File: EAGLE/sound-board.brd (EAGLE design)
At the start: 99.4 x 80 mm, 99 parts, among them IC1 SN76477, J0 POWER, J1 CON, J2 CON, J3 AUDIO, P10 1M, P2 1M, P3 1M, P4 1M, P6 50k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

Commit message: Minor modifications to PCB
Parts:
- added C27_THT: 10u, rcl:E2,5-5
- moved C27 1.27 mm to (10.2, 5.08), turned to 90 degrees
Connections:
- net GND: now also C27_THT.-
- net N$13: now also C27_THT.+
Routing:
- net N$13: track 5.40 -> 14.1 mm
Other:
- board text added: "SN76477 Sound Board 2018 Daniel Rojas"
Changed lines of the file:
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@@
 <dimension x1="0" y1="0" x2="0" y2="79.375" x3="-25.4" y3="39.6875" textsize="1.778" layer="47" visible="yes"/>
 <dimension x1="0" y1="0" x2="99.695" y2="0" x3="49.8475" y3="-19.05" textsize="1.778" layer="47" visible="yes"/>
+<text x="60.96" y="20.32" size="1.27" layer="25">SN76477 Sound Board
+2018 Daniel Rojas</text>
 </plain>
 <attributes>
@@
 <elements>
 <element name="C1" library="rcl" library_urn="urn:adsk.eagle:library:334" package="C0805" package3d_urn="urn:adsk.eagle:package:23617/2" value="150p" x="10.16" y="60.96" smashed="yes" rot="R180">
-<attribute name="VALUE" x="13.97" y="53.975" size="1.27" layer="27" rot="R180" align="bottom-right"/>
+<attribute name="VALUE" x="13.335" y="57.785" size="1.27" layer="27" rot="R180" align="bottom-right"/>
 </element>
 <element name="C10" library="rcl" library_urn="urn:adsk.eagle:library:334" package="C0805" package3d_urn="urn:adsk.eagle:package:23617/2" value="10u" x="10.16" y="45.72" smashed="yes" rot="R180">
@@
 </element>
 <element name="C2" library="rcl" library_urn="urn:adsk.eagle:library:334" package="C0805" package3d_urn="urn:adsk.eagle:package:23617/2" value="390p" x="10.16" y="63.5" smashed="yes" rot="R180">
-<attribute name="VALUE" x="13.97" y="55.88" size="1.27" layer="27" rot="R180" align="bottom-right"/>
+<attribute name="VALUE" x="13.335" y="59.69" size="1.27" layer="27" rot="R180" align="bottom-right"/>
 </element>
 <element name="C20" library="rcl" library_urn="urn:adsk.eagle:library:334" package="C0805" package3d_urn="urn:adsk.eagle:package:23617/2" value="10u" x="90.17" y="49.53" smashed="yes" rot="R180">
@@
 <attribute name="VALUE" x="86.36" y="2.54" size="1.27" layer="27" rot="R180"/>
 </element>
-<element name="C27" library="rcl" library_urn="urn:adsk.eagle:library:334" package="C0805" package3d_urn="urn:adsk.eagle:package:23617/2" value="10u" x="10.16" y="3.81" smashed="yes">
-<attribute name="VALUE" x="13.335" y="3.81" size="1.27" layer="27"/>
+<element name="C27" library="rcl" library_urn="urn:adsk.eagle:library:334" package="C0805" package3d_urn="urn:adsk.eagle:package:23617/2" value="10u" x="10.16" y="5.08" smashed="yes" rot="R90">
+<attribute name="VALUE" x="12.065" y="5.715" size="1.27" layer="27" rot="R270"/>
 </element>
 <element name="C3" library="rcl" library_urn="urn:adsk.eagle:library:334" package="C0805" package3d_urn="urn:adsk.eagle:package:23617/2" value="1n" x="10.16" y="66.04" smashed="yes" rot="R180">
-<attribute name="VALUE" x="13.97" y="57.785" size="1.27" layer="27" rot="R180" align="bottom-right"/>
+<attribute name="VALUE" x="13.335" y="67.945" size="1.27" layer="27" rot="R180" align="bottom-right"/>
 </element>
 <element name="C4" library="rcl" library_urn="urn:adsk.eagle:library:334" package="C0805" package3d_urn="urn:adsk.eagle:package:23617/2" value="10n" x="10.16" y="68.58" smashed="yes" rot="R180">
-<attribute name="VALUE" x="13.97" y="59.69" size="1.27" layer="27" rot="R180" align="bottom-right"/>
+<attribute name="VALUE" x="13.335" y="69.85" size="1.27" layer="27" rot="R180" align="bottom-right"/>
 </element>
 <element name="C5" library="rcl" library_urn="urn:adsk.eagle:library:334" package="C0805" package3d_urn="urn:adsk.eagle:package:23617/2" value="10n" x="10.16" y="33.02" smashed="yes" rot="R180">
@@
 <attribute name="VALUE" x="34.29" y="8.89" size="1.016" layer="27" ratio="10" rot="R180"/>
 </element>
+<element name="C27_THT" library="rcl" library_urn="urn:adsk.eagle:library:334" package="E2,5-5" package3d_urn="urn:adsk.eagle:package:23344/1" value="10u" x="16.51" y="5.08" smashed="yes" rot="R90"/>
 </elements>
 <signals>
@@
 </polygon>
 <via x="21.59" y="20.32" extent="1-16" drill="0.35"/>
+<contactref element="C27_THT" pad="-"/>
 </signal>
 <signal name="NOISE_OSC_RES">
@@
 <contactref element="C27" pad="1"/>
 <contactref element="CON_SPEAKER" pad="2"/>
-<wire x1="3.81" y1="3.81" x2="9.21" y2="3.81" width="0.8128" layer="1"/>
+<contactref element="C27_THT" pad="+"/>
+<wire x1="3.81" y1="3.81" x2="8.89" y2="3.81" width="0.8128" layer="1"/>
+<wire x1="8.89" y1="3.81" x2="9.84" y2="3.81" width="0.8128" layer="1"/>
+<wire x1="9.84" y1="3.81" x2="10.16" y2="4.13" width="0.8128" layer="1"/>
+<wire x1="8.89" y1="3.81" x2="16.51" y2="3.81" width="0.8128" layer="1"/>
 </signal>
 <signal name="N$60">
@@
 </drawing>
 <compatibility>
+<note version="6.3" minversion="6.2.2" severity="warning">
+Since Version 6.2.2 text objects can contain more than one line,
+which will not be processed correctly with this version.
+</note>
 <note version="8.2" severity="warning">
 Since Version 8.2, EAGLE supports online libraries. The ids

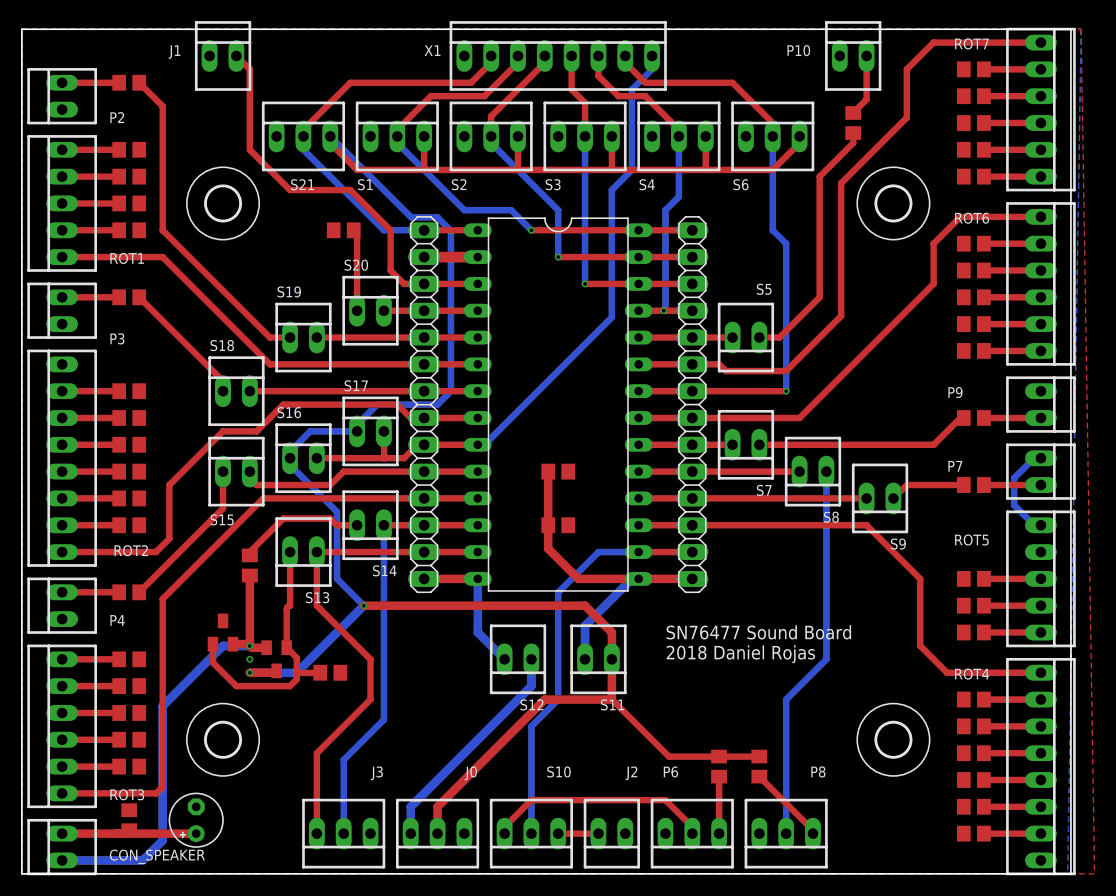
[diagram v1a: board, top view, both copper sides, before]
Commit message: Rearrange schematic components
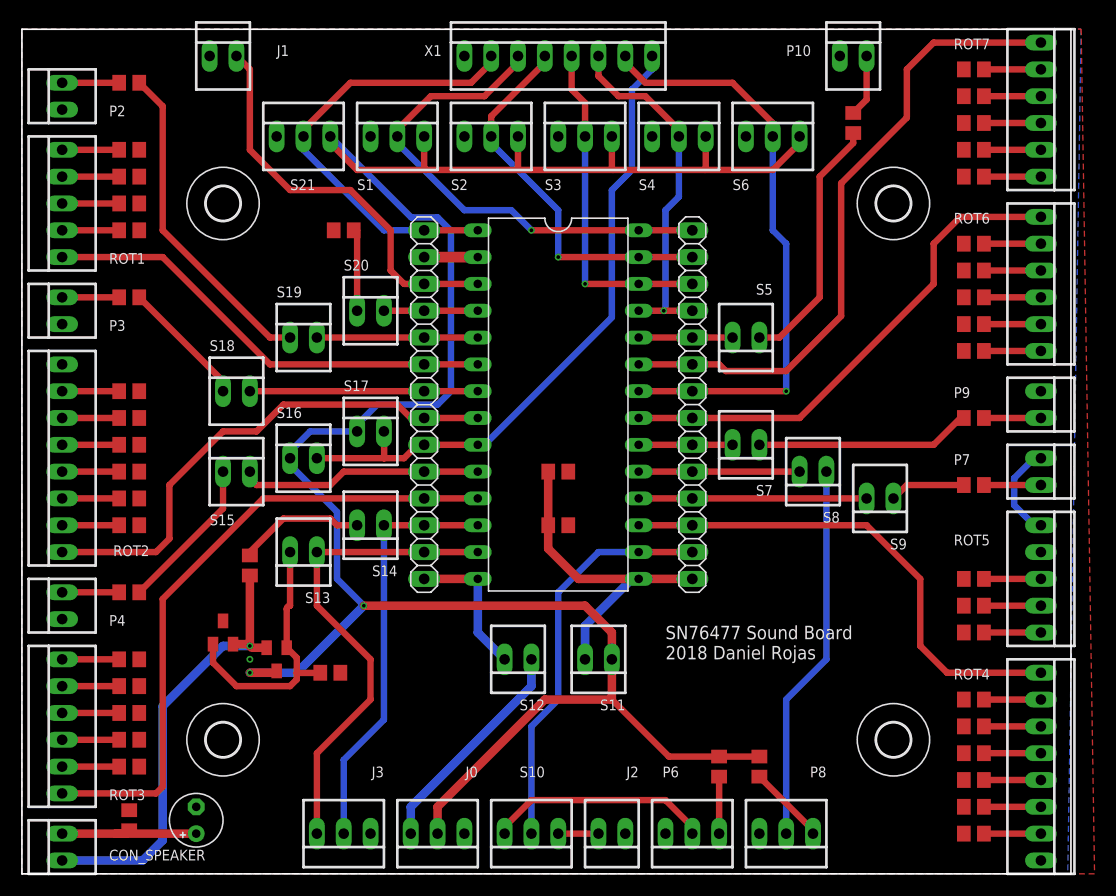
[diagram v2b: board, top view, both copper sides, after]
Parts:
- J1: value CON -> OSC_EXT
- J2: value CON -> VCO_EXT
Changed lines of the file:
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@@
 <attribute name="VALUE" x="49.8602" y="52.705" size="1.778" layer="27" ratio="10" rot="R270"/>
 </element>
-<element name="J1" library="con-molex" library_urn="urn:adsk.eagle:library:165" package="22-23-2021" value="CON" x="19.05" y="77.47" smashed="yes">
+<element name="J1" library="con-molex" library_urn="urn:adsk.eagle:library:165" package="22-23-2021" value="OSC_EXT" x="19.05" y="77.47" smashed="yes">
 <attribute name="MF" value="MOLEX" x="19.05" y="77.47" size="1.778" layer="27" display="off"/>
 <attribute name="MPN" value="22-23-2021" x="19.05" y="77.47" size="1.778" layer="27" display="off"/>
-<attribute name="NAME" x="13.97" y="77.47" size="1.016" layer="25" ratio="10"/>
+<attribute name="NAME" x="24.13" y="77.47" size="1.016" layer="25" ratio="10"/>
 <attribute name="OC_FARNELL" value="1462926" x="19.05" y="77.47" size="1.778" layer="27" display="off"/>
 <attribute name="OC_NEWARK" value="25C3832" x="19.05" y="77.47" size="1.778" layer="27" display="off"/>
-</element>
-<element name="J2" library="con-molex" library_urn="urn:adsk.eagle:library:165" package="22-23-2021" value="CON" x="55.88" y="3.81" smashed="yes" rot="R180">
+<attribute name="VALUE" x="24.13" y="75.565" size="1.016" layer="27" ratio="10"/>
+</element>
+<element name="J2" library="con-molex" library_urn="urn:adsk.eagle:library:165" package="22-23-2021" value="VCO_EXT" x="55.88" y="3.81" smashed="yes" rot="R180">
 <attribute name="MF" value="MOLEX" x="55.88" y="3.81" size="1.778" layer="27" rot="R180" display="off"/>
 <attribute name="MPN" value="22-23-2021" x="55.88" y="3.81" size="1.778" layer="27" rot="R180" display="off"/>
@@
 <attribute name="MF" value="MOLEX" x="3.81" y="73.66" size="1.778" layer="27" rot="R90" display="off"/>
 <attribute name="MPN" value="22-23-2021" x="3.81" y="73.66" size="1.778" layer="27" rot="R90" display="off"/>
-<attribute name="NAME" x="8.255" y="71.12" size="1.016" layer="25" ratio="10"/>
+<attribute name="NAME" x="8.255" y="71.755" size="1.016" layer="25" ratio="10"/>
 <attribute name="OC_FARNELL" value="1462926" x="3.81" y="73.66" size="1.778" layer="27" rot="R90" display="off"/>
 <attribute name="OC_NEWARK" value="25C3832" x="3.81" y="73.66" size="1.778" layer="27" rot="R90" display="off"/>
-<attribute name="VALUE" x="10.795" y="71.12" size="1.016" layer="27" ratio="10"/>
+<attribute name="VALUE" x="10.795" y="71.755" size="1.016" layer="27" ratio="10"/>
 </element>
 <element name="P3" library="con-molex" library_urn="urn:adsk.eagle:library:165" package="22-23-2021" value="1M" x="3.81" y="53.34" smashed="yes" rot="R90">
 <attribute name="MF" value="MOLEX" x="3.81" y="53.34" size="1.778" layer="27" rot="R90" display="off"/>
 <attribute name="MPN" value="22-23-2021" x="3.81" y="53.34" size="1.778" layer="27" rot="R90" display="off"/>
-<attribute name="NAME" x="8.255" y="50.165" size="1.016" layer="25" ratio="10"/>
+<attribute name="NAME" x="8.255" y="51.435" size="1.016" layer="25" ratio="10"/>
 <attribute name="OC_FARNELL" value="1462926" x="3.81" y="53.34" size="1.778" layer="27" rot="R90" display="off"/>
 <attribute name="OC_NEWARK" value="25C3832" x="3.81" y="53.34" size="1.778" layer="27" rot="R90" display="off"/>
-<attribute name="VALUE" x="10.795" y="50.165" size="1.016" layer="27" ratio="10"/>
+<attribute name="VALUE" x="10.795" y="51.435" size="1.016" layer="27" ratio="10"/>
 </element>
 <element name="P4" library="con-molex" library_urn="urn:adsk.eagle:library:165" package="22-23-2021" value="1M" x="3.81" y="25.4" smashed="yes" rot="R90">
@@
 <attribute name="MF" value="MOLEX" x="96.52" y="38.1" size="1.778" layer="27" rot="R270" display="off"/>
 <attribute name="MPN" value="22-23-2021" x="96.52" y="38.1" size="1.778" layer="27" rot="R270" display="off"/>
-<attribute name="NAME" x="87.63" y="38.1" size="1.016" layer="25" ratio="10"/>
+<attribute name="NAME" x="88.265" y="38.735" size="1.016" layer="25" ratio="10"/>
 <attribute name="OC_FARNELL" value="1462926" x="96.52" y="38.1" size="1.778" layer="27" rot="R270" display="off"/>
 <attribute name="OC_NEWARK" value="25C3832" x="96.52" y="38.1" size="1.778" layer="27" rot="R270" display="off"/>
-<attribute name="VALUE" x="90.17" y="38.1" size="1.016" layer="27" ratio="10"/>
+<attribute name="VALUE" x="90.805" y="38.735" size="1.016" layer="27" ratio="10"/>
 </element>
 <element name="P8" library="con-molex" library_urn="urn:adsk.eagle:library:165" package="22-23-2031" value="50k" x="72.39" y="3.81" smashed="yes" rot="R180">
@@
 <attribute name="MF" value="MOLEX" x="96.52" y="44.45" size="1.778" layer="27" rot="R270" display="off"/>
 <attribute name="MPN" value="22-23-2021" x="96.52" y="44.45" size="1.778" layer="27" rot="R270" display="off"/>
-<attribute name="NAME" x="87.63" y="45.085" size="1.016" layer="25" ratio="10"/>
+<attribute name="NAME" x="88.265" y="45.085" size="1.016" layer="25" ratio="10"/>
 <attribute name="OC_FARNELL" value="1462926" x="96.52" y="44.45" size="1.778" layer="27" rot="R270" display="off"/>
 <attribute name="OC_NEWARK" value="25C3832" x="96.52" y="44.45" size="1.778" layer="27" rot="R270" display="off"/>
-<attribute name="VALUE" x="90.17" y="45.085" size="1.016" layer="27" ratio="10"/>
+<attribute name="VALUE" x="90.805" y="45.085" size="1.016" layer="27" ratio="10"/>
 </element>
 <element name="R1" library="rcl" library_urn="urn:adsk.eagle:library:334" package="R0805" package3d_urn="urn:adsk.eagle:package:23553/2" value="47k" x="30.48" y="60.96" smashed="yes">
@@
 </element>
 <element name="R11" library="rcl" library_urn="urn:adsk.eagle:library:334" package="R0805" package3d_urn="urn:adsk.eagle:package:23553/2" value="2.7k" x="90.17" y="43.18" smashed="yes" rot="R180">
-<attribute name="VALUE" x="92.075" y="41.275" size="1.27" layer="27" rot="R180"/>
+<attribute name="VALUE" x="87.63" y="43.815" size="1.27" layer="27" rot="R180"/>
 </element>
 <element name="R12" library="rcl" library_urn="urn:adsk.eagle:library:334" package="R0805" package3d_urn="urn:adsk.eagle:package:23553/2" value="100k" x="90.17" y="27.94" smashed="yes">
@@
 </element>
 <element name="R16" library="rcl" library_urn="urn:adsk.eagle:library:334" package="R0805" package3d_urn="urn:adsk.eagle:package:23553/2" value="2.7k" x="90.17" y="36.83" smashed="yes" rot="R180">
-<attribute name="VALUE" x="92.075" y="35.56" size="1.27" layer="27" rot="R180"/>
+<attribute name="VALUE" x="87.63" y="37.465" size="1.27" layer="27" rot="R180"/>
 </element>
 <element name="R17" library="rcl" library_urn="urn:adsk.eagle:library:334" package="R0805" package3d_urn="urn:adsk.eagle:package:23553/2" value="50k" x="66.04" y="10.16" smashed="yes" rot="R270">
@@
 </element>
 <element name="R3" library="rcl" library_urn="urn:adsk.eagle:library:334" package="R0805" package3d_urn="urn:adsk.eagle:package:23553/2" value="2.7k" x="10.16" y="54.61" smashed="yes">
-<attribute name="VALUE" x="9.525" y="52.07" size="1.27" layer="27"/>
+<attribute name="VALUE" x="13.335" y="53.975" size="1.27" layer="27"/>
 </element>
 <element name="R4" library="rcl" library_urn="urn:adsk.eagle:library:334" package="R0805" package3d_urn="urn:adsk.eagle:package:23553/2" value="2.7k" x="10.16" y="26.67" smashed="yes">
@@
 <attribute name="MF" value="MOLEX" x="48.26" y="3.81" size="1.778" layer="27" rot="R180" display="off"/>
 <attribute name="MPN" value="22-23-2031" x="48.26" y="3.81" size="1.778" layer="27" rot="R180" display="off"/>
-<attribute name="NAME" x="52.07" y="10.16" size="1.016" layer="25" ratio="10" rot="R180"/>
+<attribute name="NAME" x="49.53" y="10.16" size="1.016" layer="25" ratio="10" rot="R180"/>
 <attribute name="OC_FARNELL" value="1462950" x="48.26" y="3.81" size="1.778" layer="27" rot="R180" display="off"/>
 <attribute name="OC_NEWARK" value="30C0862" x="48.26" y="3.81" size="1.778" layer="27" rot="R180" display="off"/>
-<attribute name="VALUE" x="52.07" y="8.89" size="1.016" layer="27" ratio="10" rot="R180"/>
+<attribute name="VALUE" x="49.53" y="8.89" size="1.016" layer="27" ratio="10" rot="R180"/>
 </element>
 <element name="S11" library="con-molex" library_urn="urn:adsk.eagle:library:165" package="22-23-2021" value="SPST" x="54.61" y="20.32" smashed="yes" rot="R180">
